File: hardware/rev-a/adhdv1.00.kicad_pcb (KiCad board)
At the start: 2 copper layers, 60 x 40 mm, 66 parts, among them J1 USB_C_Receptacle_PowerOnly_6P, J10 Conn_01x05, J11 Conn_01x04, J12 Conn_01x05, J13 Conn_01x04, J14 Conn_01x04, J15 Conn_01x04, J16 Conn_01x02, J2 Conn_01x02, Q1 NPN, SW1 SW_Push, U1 BQ24074RGT, U2 TLV75533PDBV, U3 MDBT42Q-512K, U4 DS3231MZ, U5 DRV2605LDGS

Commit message: updated layout from schematic
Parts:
- removed J11: Conn_01x04, Connector_PinHeader_2.54mm:PinHeader_1x04_P2.54mm_Vertical
- removed J12: Conn_01x05, Connector_JST:JST_PH_B5B-PH-K_1x05_P2.00mm_Vertical
- removed Q1: NPN, Package_TO_SOT_SMD:SOT-23
- added C16: 0.1uF, Capacitor_SMD:C_0603_1608Metric, F.Cu at (28.1, 84.9)
- added C17: 0.1uF, Capacitor_SMD:C_0603_1608Metric, F.Cu at (32.1, 69.8)
- added C18: 0.1uF, Capacitor_SMD:C_0603_1608Metric, F.Cu at (32.1, 72.4)
- added C19: 0.1uF, Capacitor_SMD:C_0603_1608Metric, F.Cu at (32.1, 74.9)
- added C20: 0.1uF, Capacitor_SMD:C_0603_1608Metric, F.Cu at (32.1, 77.4)
- added C21: 0.1uF, Capacitor_SMD:C_0603_1608Metric, F.Cu at (45.1, 43.8)
- added C22: 0.1uF, Capacitor_SMD:C_0603_1608Metric, F.Cu at (45.1, 46.3)
- added H1: MountingHole, MountingHole:MountingHole_2.2mm_M2_Pad, F.Cu at (78.2, 21.0)
- added H2: MountingHole, MountingHole:MountingHole_2.2mm_M2_Pad, F.Cu at (78.2, 26.9)
- added H3: MountingHole, MountingHole:MountingHole_2.2mm_M2_Pad, F.Cu at (78.2, 32.9)
- added H4: MountingHole, MountingHole:MountingHole_2.2mm_M2_Pad, F.Cu at (78.2, 38.8)
- added J3: Conn_01x03, Connector_PinHeader_2.54mm:PinHeader_1x03_P2.54mm_Vertical, F.Cu at (69.7, 20.3)
- added J4: Conn_01x04, Connector_PinHeader_2.54mm:PinHeader_1x04_P2.54mm_Vertical, F.Cu at (65.1, 20.3)
- added Q2: MMBT2222A_RFG, Package_TO_SOT_SMD:SOT-23, F.Cu at (49.5, 64.4)
- added R24: 10K, Resistor_SMD:R_0603_1608Metric, F.Cu at (36.1, 84.9)
- added R25: 100, Resistor_SMD:R_0603_1608Metric, F.Cu at (53.1, 48.8)
- BT1: footprint Battery:BatteryHolder_Keystone_103_1x20mm -> Battery:BatteryHolder_Keystone_3034_1x20mm; moved to F.Cu
- BZ1: footprint TerminalBlock:TerminalBlock_MaiXu_MX126-5.0-02P_1x02_P5.00mm -> CMT-1203-SMT:CUI_CMT-1203-SMT; moved to F.Cu
- C1, C4, D1, R3, R4: moved to F.Cu
- J1: footprint Connector_USB:USB_C_Receptacle_HRO_TYPE-C-31-M-12 -> Connector_USB:USB_C_Receptacle_GCT_USB4105-xx-A_16P_TopMnt_Horizontal
- SW1: footprint Button_Switch_SMD:SW_SPST_TL3342 -> Button_Switch_SMD:SW_SPST_EVQP0
- U1: footprint Package_DFN_QFN:VQFN-16-1EP_3x3mm_P0.5mm_EP1.6x1.6mm -> BQ24074RGTRG4:QFN50P300X300X100-17N
- U5: footprint Package_SO:VSSOP-10_3x3mm_P0.5mm -> DRV2605LDGST:SOP50P490X110-10N; moved to F.Cu
- moved U5 141.2 mm to (51.2, 59.9), turned to 0 degrees
- moved J16 129.4 mm to (42.1, 60.3)
- moved D1 119.2 mm to (67.0, 64.8), turned to 0 degrees
- moved J15 118.3 mm to (53.9, 33.8), turned to 0 degrees
- moved J14 118.2 mm to (53.9, 27.3), turned to 0 degrees
- moved J13 118.1 mm to (53.9, 20.7), turned to 0 degrees
- moved U3 113.8 mm to (32.6, 49.5)
- moved BT1 110.0 mm to (38.5, 29.0), turned to 0 degrees
- moved BZ1 106.7 mm to (61.9, 48.3), turned to 0 degrees
- moved U2 105.7 mm to (48.6, 86.3)
- moved C4 98.3 mm to (28.1, 77.4), turned to 0 degrees
- moved C1 94.2 mm to (28.1, 69.8)
- moved R3 93.0 mm to (32.1, 84.9), turned to 0 degrees
- moved R4 86.3 mm to (36.1, 69.8), turned to 0 degrees
- moved U1 80.1 mm to (49.2, 81.3), turned to 0 degrees
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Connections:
- BZ1 pad 2: Net-(BZ1--) -> +3V3
- C1 pad 1: GND -> VBUS
- C1 pad 2: VBUS -> GND
- C15 pad 1: /MCU/VBAT_ADC -> GND
- C15 pad 2: GND -> /MCU/VBAT_ADC
- C2 pad 1: VSYS -> GND
- C2 pad 2: GND -> VSYS
- C3 pad 1: GND -> +3V3
- C3 pad 2: +3V3 -> GND
- C5 pad 1: VSYS -> GND
- C5 pad 2: GND -> VSYS
- C6 pad 1: VBAT -> GND
- C6 pad 2: GND -> VBAT
- D1 pad 1: Net-(BZ1--) -> +3V3
- U1 pad 5: VBUS -> GND
- U1 pad 6: GND -> Net-(U1-EN1)
- U2 pad 1: GND -> VSYS
- U2 pad 3: GND -> VSYS
- U3 pad 17: /MCU/VBAT_ADC -> Net-(U3-AIN2/P0.04)
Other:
- board outline removed

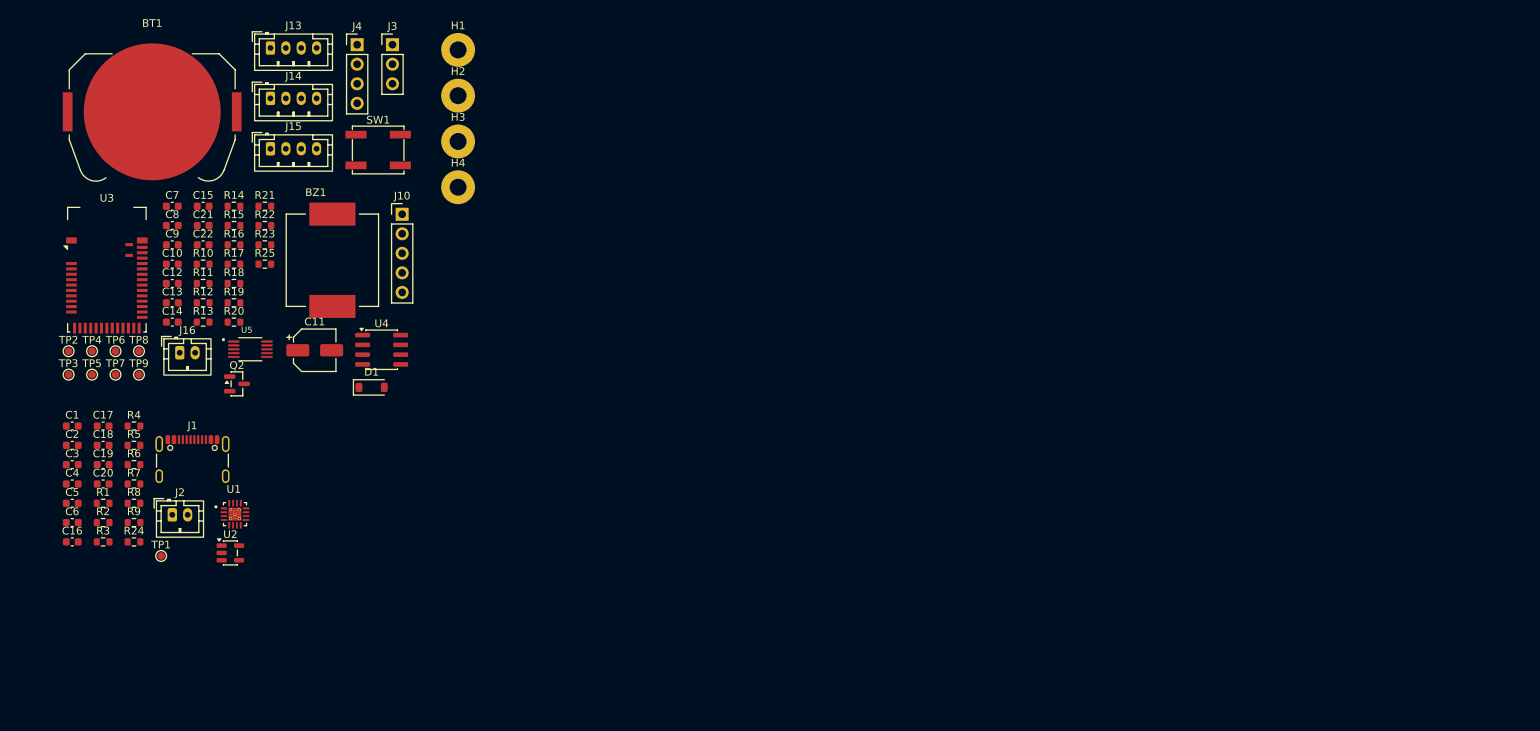
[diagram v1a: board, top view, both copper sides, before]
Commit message: format schematic to fit convention, replace SWD header with 2x5
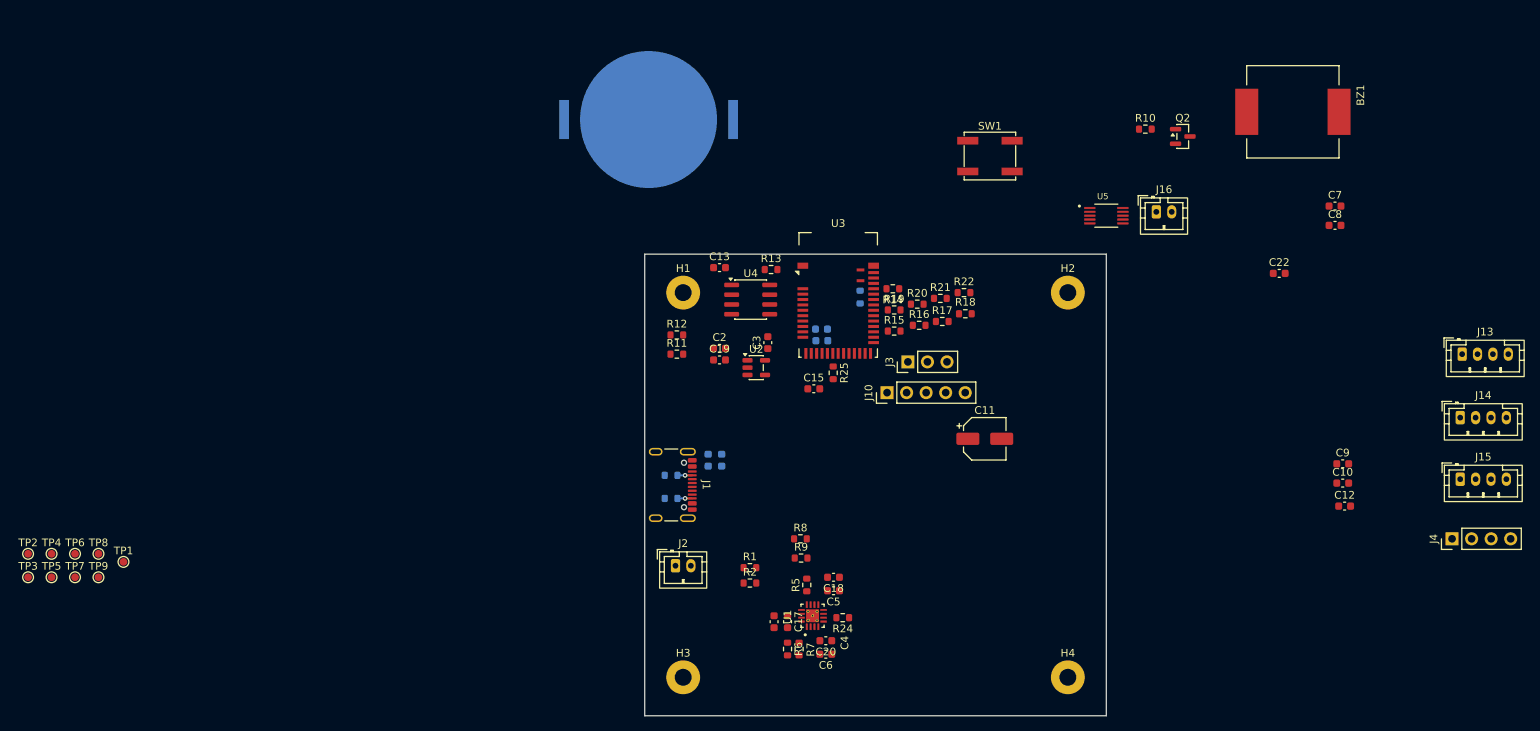
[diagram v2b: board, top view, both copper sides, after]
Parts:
- removed D1: D, Diode_SMD:D_SOD-123
- BT1, C1, C14, C16, C21, R23, R3, R4: moved to B.Cu
- moved J15 160.5 mm to (208.5, 76.8)
- moved J14 160.1 mm to (208.5, 68.8)
- moved J13 159.9 mm to (208.8, 60.5)
- moved J4 156.1 mm to (207.4, 84.5), turned to 90 degrees
- moved C12 155.1 mm to (193.5, 80.2)
- moved C10 154.8 mm to (193.2, 77.3)
- moved C9 154.8 mm to (193.2, 74.8)
- moved C7 151.1 mm to (192.2, 41.2)
- moved C8 151.1 mm to (192.2, 43.8)
- moved C22 139.9 mm to (185.0, 50.0)
- moved J16 128.2 mm to (169.0, 42.0)
- moved Q2 127.1 mm to (172.4, 32.2)
- moved BZ1 126.3 mm to (186.8, 29.0), turned to -90 degrees
- moved R10 123.7 mm to (167.6, 31.2)
- moved U5 112.6 mm to (162.5, 42.5)
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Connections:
- BZ1 pad 2: +3V3 -> Net-(BZ1--)
- J10 pad 1: +3V3 -> GND
- J10 pad 5: GND -> +3V3
- J3 pad 1: /MCU/UART_RX -> GND
- J3 pad 2: /MCU/UART_TX -> /MCU/UART_RX
- J3 pad 3: GND -> /MCU/UART_TX
- J4 pad 1: /MCU/BTN1 -> GND
- J4 pad 2: /MCU/BTN2 -> /MCU/BTN1
- J4 pad 3: /MCU/BTN3 -> /MCU/BTN2
- J4 pad 4: GND -> /MCU/BTN3
- Q2 pad 3: +3V3 -> Net-(BZ1--)
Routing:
- net Net-(J1-CC2): track 0.00 -> 1.93 mm, vias 0 -> 1
- net Net-(J1-CC1): track 0.00 -> 1.93 mm, vias 0 -> 1
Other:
- board outline added: 60 x 60 mm

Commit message: crackhead layout file added
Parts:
- removed J13, J14, J15: Conn_01x04, Connector_JST:JST_PH_B4B-PH-K_1x04_P2.00mm_Vertical
- removed J16: Conn_01x02, Connector_JST:JST_PH_B2B-PH-K_1x02_P2.00mm_Vertical
- removed J4: Conn_01x04, Connector_PinHeader_2.54mm:PinHeader_1x04_P2.54mm_Vertical
- removed Q2: MMBT2222A_RFG, Package_TO_SOT_SMD:SOT-23
- added C23: 220uF, Capacitor_SMD:C_0603_1608Metric, B.Cu at (151.2, 86.3)
- added C24: 0.1uF, Capacitor_SMD:C_0603_1608Metric, B.Cu at (152.8, 86.3)
- added J5: Conn_01x03, Connector_PinHeader_2.54mm:PinHeader_1x03_P2.54mm_Vertical, F.Cu at (125.0, 63.0)
- added J6: Conn_01x04, Connector_PinHeader_2.54mm:PinHeader_1x04_P2.54mm_Vertical, F.Cu at (101.2, 56.7)
- added J7: Conn_01x04, Connector_JST:JST_PH_B4B-PH-K_1x04_P2.00mm_Vertical, F.Cu at (155.4, 63.5)
- added J8: Conn_01x04, Connector_JST:JST_PH_B4B-PH-K_1x04_P2.00mm_Vertical, F.Cu at (155.5, 75.0)
- added J9: Conn_01x04, Connector_JST:JST_PH_B4B-PH-K_1x04_P2.00mm_Vertical, F.Cu at (155.5, 86.5)
- added Q1: MMBT2222A_RFG, Package_TO_SOT_SMD:SOT-23, F.Cu at (133.9, 91.7)
- added R26: 100, Resistor_SMD:R_0603_1608Metric, F.Cu at (105.1, 61.8)
- added R27: 100, Resistor_SMD:R_0603_1608Metric, F.Cu at (105.1, 59.3)
- C1: value 10uF -> 0.1uF
- C10: value 0.1uF -> 4.7uF; moved to B.Cu
- C11: value 220uF -> 0.1uF; footprint Capacitor_SMD:CP_Elec_5x5.4 -> Capacitor_SMD:C_0603_1608Metric; moved to B.Cu
- C12: value 0.1uF -> 1uF; moved to B.Cu
- C13, C15, C17, C20, C22, C3: moved to B.Cu
- C14: value 10uF -> 1uF; moved to F.Cu
- C16: value 0.1uF -> 10uF
- C19: value 0.1uF -> 47uF; moved to B.Cu
- C2: value 1uF -> 10uF; moved to B.Cu
- C21: value 0.1uF -> 47uF
- C4: value 10uF -> 0.1uF; moved to B.Cu
- C5: value 4.7uF -> 1uF
- C6: value 4.7uF -> 10uF; moved to B.Cu
- C7: value 1uF -> 0.1uF; moved to B.Cu
- C8: value 1uF -> 4.7uF; moved to B.Cu
- C9: value 47uF -> 0.1uF; moved to B.Cu
- J1: footprint Connector_USB:USB_C_Receptacle_GCT_USB4105-xx-A_16P_TopMnt_Horizontal -> USB4515-GF-A_REVA:GCT_USB4515-GF-A_REVA
- J10: value Conn_01x05 -> 3220-10-0300-00; footprint Connector_PinHeader_2.54mm:PinHeader_1x05_P2.54mm_Vertical -> Connector_PinHeader_1.27mm:PinHeader_2x05_P1.27mm_Vertical
- J3: value Conn_01x03 -> Conn_01x02; footprint Connector_PinHeader_2.54mm:PinHeader_1x03_P2.54mm_Vertical -> Connector_JST:JST_PH_B2B-PH-K_1x02_P2.00mm_Vertical
- R1, R2: value 100k -> 5.1k
- R10: value 1k -> 10k
- R11, R12: value 4.7k -> 10k
- R13, R14: value 10k -> 4.7k
- R15, R17: value 100 -> 10k
- R16: value 100 -> 1k
- R23: moved to F.Cu
- R24: value 10K -> 100
- R3: value 5.1k -> 10k; moved to F.Cu
- R4: value 5.1k -> 100k; moved to F.Cu
- R5: value 3k -> 100k
- R6: value 1.8k -> 3k
- R7: value 10k -> 10K
- R8: value 10k -> 1.8k
- U1: value BQ24074RGT -> TLV75533PDBV; footprint BQ24074RGTRG4:QFN50P300X300X100-17N -> Package_TO_SOT_SMD:SOT-23-5
- U2: value TLV75533PDBV -> BQ24074RGT; footprint Package_TO_SOT_SMD:SOT-23-5 -> BQ24074RGTRG4:QFN50P300X300X100-17N
- U3: value MDBT42Q-512K -> DRV2605LDGS; footprint RF_Module:Raytac_MDBT42Q -> DRV2605LDGST:SOP50P490X110-10N
- U5: value DRV2605LDGS -> MDBT42Q-512K; footprint DRV2605LDGST:SOP50P490X110-10N -> RF_Module:Raytac_MDBT42Q
- moved C7 82.2 mm to (117.2, 75.0), turned to -90 degrees
- moved C10 79.6 mm to (113.8, 82.0), turned to -90 degrees
- moved C8 78.6 mm to (119.2, 73.0), turned to -90 degrees
- moved C12 78.3 mm to (116.5, 94.5), turned to 90 degrees
- moved BZ1 72.6 mm to (142.5, 86.5), turned to 0 degrees
- moved C9 72.5 mm to (120.8, 73.0), turned to -90 degrees
- moved TP2 67.1 mm to (88.8, 76.8)
- moved BT1 62.3 mm to (129.2, 86.5)
- moved R10 59.8 mm to (128.2, 76.2)
- moved TP1 54.2 mm to (88.5, 80.8)
- moved J3 48.1 mm to (111.5, 102.5), turned to 0 degrees
- moved C13 45.4 mm to (115.0, 94.5), turned to 90 degrees
- moved U3 45.3 mm to (119.0, 97.2), turned to 180 degrees
- moved C20 44.5 mm to (152.5, 62.0), turned to 90 degrees
- moved R24 43.1 mm to (149.9, 57.5)
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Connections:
- C10 pad 1: VBAT -> GND
- C10 pad 2: GND -> VBAT
- C11 pad 1: VBAT -> GND
- C11 pad 2: GND -> VBAT
- C13 pad 1: GND -> VBAT
- C13 pad 2: +3V3 -> GND
- C14 pad 1: GND -> Net-(U3-REG)
- C14 pad 2: +3V3 -> GND
- C15 pad 1: GND -> +3V3
- C15 pad 2: /MCU/VBAT_ADC -> GND
- C16 pad 1: VBUS -> +3V3
- C17 pad 1: VBUS -> +3V3
- C18 pad 2: VSYS -> /MCU/VBAT_ADC
- C19 pad 1: GND -> VBAT
- C19 pad 2: VSYS -> GND
- C2 pad 1: GND -> VBUS
- C2 pad 2: VSYS -> GND
- C20 pad 1: GND -> VBAT
- C20 pad 2: VBAT -> GND
- C21 pad 1: GND -> VBAT
- C21 pad 2: +3V3 -> GND
- C22 pad 1: GND -> VBAT
- C22 pad 2: +3V3 -> GND
- C3 pad 1: +3V3 -> GND
- C3 pad 2: GND -> VSYS
- C4 pad 1: VBUS -> GND
- C4 pad 2: GND -> VSYS
- C5 pad 1: GND -> +3V3
- C5 pad 2: VSYS -> GND
- C6 pad 2: VBAT -> VBUS
- C7 pad 2: +3V3 -> VBUS
- C8 pad 1: Net-(U5-REG) -> GND
- C8 pad 2: GND -> VSYS
- C9 pad 1: VBAT -> GND
- C9 pad 2: GND -> VSYS
- J10 pad 1: GND -> +3V3
- J10 pad 3: /MCU/SWDCLK -> GND
- J10 pad 4: /MCU/RESET -> /MCU/SWDCLK
- J10 pad 5: +3V3 -> GND
- J3 pad 1: GND -> Net-(J3-Pin_1)
- J3 pad 2: /MCU/UART_RX -> Net-(J3-Pin_2)
- R1 pad 1: VBAT -> Net-(J1-CC2)
- R1 pad 2: /MCU/VBAT_ADC -> GND
- R10 pad 1: /MCU/BUZZ_PWM -> /MCU/PGOOD_STAT
- R10 pad 2: Net-(Q2-Pad1) -> +3V3
- R11 pad 2: /MCU/SCL -> /MCU/CHG_STAT
- R12 pad 2: /MCU/SDA -> Net-(U3-EN)
- R13 pad 1: +3V3 -> /MCU/SDA
- R13 pad 2: /MCU/INT/SQW -> +3V3
- R14 pad 1: +3V3 -> /MCU/SCL
- R14 pad 2: /MCU/RESET -> +3V3
- R15 pad 1: Net-(U3-P0.13) -> /MCU/INT/SQW
- R15 pad 2: /MCU/BTN1 -> +3V3
- R16 pad 1: Net-(U3-TRACEDATA3/P0.14) -> /MCU/BUZZ_PWM
- R16 pad 2: /MCU/BTN2 -> Net-(Q1-Pad1)
- R17 pad 1: Net-(U3-TRACEDATA2/P0.15) -> +3V3
- R17 pad 2: /MCU/BTN3 -> /MCU/RESET
- R18 pad 1: /MCU/LED1_DATA -> Net-(U5-AIN2/P0.04)
- R18 pad 2: Net-(U3-TRACEDATA1/P0.16) -> /MCU/VBAT_ADC
- R19 pad 1: /MCU/LED1_CLK -> Net-(U5-P0.12)
- R19 pad 2: Net-(U3-P0.17) -> /MCU/LED3_DATA
- R2 pad 2: /MCU/VBAT_ADC -> Net-(J1-CC1)
- R20 pad 1: /MCU/LED2_DATA -> Net-(U5-P0.13)
- R20 pad 2: Net-(U3-TRACEDATA0/P0.18) -> /MCU/LED3_CLK
- R21 pad 1: /MCU/LED2_CLK -> Net-(U5-TRACEDATA3/P0.14)
- R21 pad 2: Net-(U3-P0.19) -> /MCU/LED2_DATA
- R22 pad 1: /MCU/LED3_DATA -> /MCU/LED2_CLK
- R22 pad 2: Net-(U3-TRACECLK/P0.20) -> Net-(U5-TRACEDATA2/P0.15)
- R23 pad 1: /MCU/LED3_CLK -> /MCU/LED1_DATA
- R23 pad 2: Net-(U3-P0.23) -> Net-(U5-TRACEDATA1/P0.16)
- R24 pad 1: VBUS -> /MCU/LED1_CLK
- R24 pad 2: Net-(U1-EN1) -> Net-(U5-P0.17)
- R25 pad 1: Net-(U3-AIN2/P0.04) -> /MCU/BTN3
- R25 pad 2: /MCU/VBAT_ADC -> Net-(U5-TRACEDATA0/P0.18)
- R3 pad 1: Net-(J1-CC1) -> VSYS
- R3 pad 2: GND -> Net-(U1-EN)
- R4 pad 1: Net-(J1-CC2) -> /MCU/VBAT_ADC
- R4 pad 2: GND -> VBAT
- R5 pad 1: Net-(U1-ILIM) -> GND
- R5 pad 2: GND -> /MCU/VBAT_ADC
- R6 pad 1: Net-(U1-ISET) -> Net-(U2-ILIM)
- R7 pad 1: Net-(U1-TS) -> Net-(U2-EN1)
- R7 pad 2: GND -> VBUS
- R8 pad 1: +3V3 -> Net-(U2-ISET)
- R8 pad 2: /MCU/PGOOD_STAT -> GND
- R9 pad 1: +3V3 -> Net-(U2-TS)
- R9 pad 2: /MCU/CHG_STAT -> GND
- TP2 pad 1: /MCU/SWDIO -> +3V3
- TP3 pad 1: /MCU/SWDCLK -> /MCU/SDA
- TP4 pad 1: /MCU/RESET -> /MCU/SCL
- TP5 pad 1: +3V3 -> /MCU/BUZZ_PWM
- TP7 pad 1: /MCU/BUZZ_PWM -> /MCU/RESET
- TP8 pad 1: /MCU/SDA -> /MCU/SWDCLK
- TP9 pad 1: /MCU/SCL -> /MCU/SWDIO
- U1 pad 1: Net-(U1-TS) -> VSYS
- U1 pad 2: VBAT -> GND
- U1 pad 3: VBAT -> Net-(U1-EN)
- U1 pad 4: GND -> unconnected-(U1-NC-Pad4)
- U1 pad 5: GND -> +3V3
- U2 pad 1: VSYS -> Net-(U2-TS)
- U2 pad 2: GND -> VBAT
- U2 pad 3: VSYS -> VBAT
- U2 pad 4: unconnected-(U2-NC-Pad4) -> GND
- U2 pad 5: +3V3 -> GND
- U3 pad 1: GND -> Net-(U3-REG)
- U3 pad 10: unconnected-(U3-DCC-Pad10) -> VBAT
- U3 pad 2: unconnected-(U3-P0.25-Pad2) -> /MCU/SCL
- U3 pad 4: /MCU/SCL -> GND
- U3 pad 5: unconnected-(U3-AIN4/P0.28-Pad5) -> Net-(U3-EN)
- U3 pad 6: unconnected-(U3-AIN5/P0.29-Pad6) -> VBAT
- U3 pad 7: unconnected-(U3-AIN6/P0.30-Pad7) -> Net-(J3-Pin_1)
- U3 pad 8: unconnected-(U3-AIN7/P0.31-Pad8) -> GND
- U3 pad 9: unconnected-(U3-DEC4-Pad9) -> Net-(J3-Pin_2)
- U5 pad 1: Net-(U5-REG) -> GND
- U5 pad 10: +3V3 -> unconnected-(U5-DCC-Pad10)
- U5 pad 2: /MCU/SCL -> /MCU/SDA
- U5 pad 3: /MCU/SDA -> /MCU/SCL
- U5 pad 4: GND -> unconnected-(U5-P0.27-Pad4)
- U5 pad 5: +3V3 -> unconnected-(U5-AIN4/P0.28-Pad5)
- U5 pad 6: +3V3 -> unconnected-(U5-AIN5/P0.29-Pad6)
- U5 pad 7: Net-(J16-Pin_1) -> unconnected-(U5-AIN6/P0.30-Pad7)
- U5 pad 8: GND -> unconnected-(U5-AIN7/P0.31-Pad8)
- U5 pad 9: Net-(J16-Pin_2) -> unconnected-(U5-DEC4-Pad9)
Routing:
- net VBAT: track 0.00 -> 148.0 mm, vias 0 -> 1
- net +3V3: track 0.00 -> 111.7 mm, vias 0 -> 2
- net Net-(BT1-+): track 0.00 -> 95.1 mm, vias 0 -> 1
- net /MCU/SCL: track 0.00 -> 62.4 mm, vias 0 -> 2
- net /MCU/SDA: track 0.00 -> 57.6 mm, vias 0 -> 3
- net /MCU/RESET: track 0.00 -> 47.1 mm
- net /MCU/VBAT_ADC: track 0.00 -> 41.4 mm, vias 0 -> 4
- net Net-(U5-TRACEDATA0/P0.18): track 0.00 -> 37.4 mm, vias 0 -> 2
- net Net-(U5-P0.19): track 0.00 -> 35.6 mm, vias 0 -> 2
- net Net-(U5-TRACECLK/P0.20): track 0.00 -> 35.3 mm, vias 0 -> 2
- net VBUS: track 0.00 -> 32.5 mm, vias 0 -> 4
- net /MCU/BUZZ_PWM: track 0.00 -> 32.2 mm, vias 0 -> 2
- net Net-(U5-TRACEDATA3/P0.14): track 0.00 -> 25.1 mm, vias 0 -> 2
- net Net-(U5-TRACEDATA2/P0.15): track 0.00 -> 24.4 mm, vias 0 -> 2
- net Net-(U5-P0.12): track 0.00 -> 24.0 mm, vias 0 -> 2
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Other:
- outline, holes or cut-outs redrawn
- rule pad_to_mask_clearance: 0 -> 0.1
